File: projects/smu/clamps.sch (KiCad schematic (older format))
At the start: 39 parts, among them U401 DAC8734, U402 LM324, U404 LM324, U405 DG444

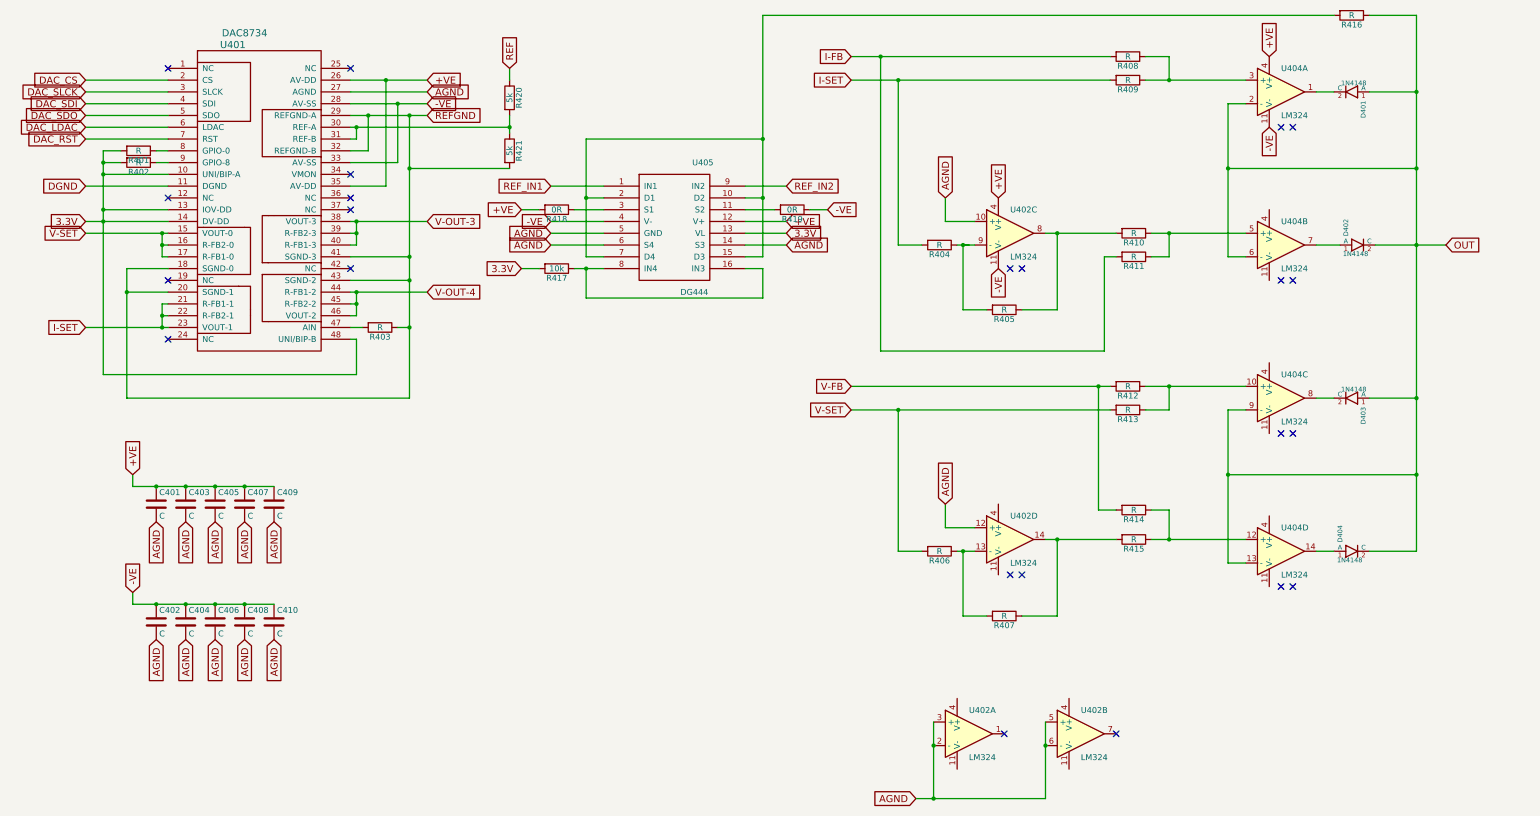
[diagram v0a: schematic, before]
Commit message: add output section
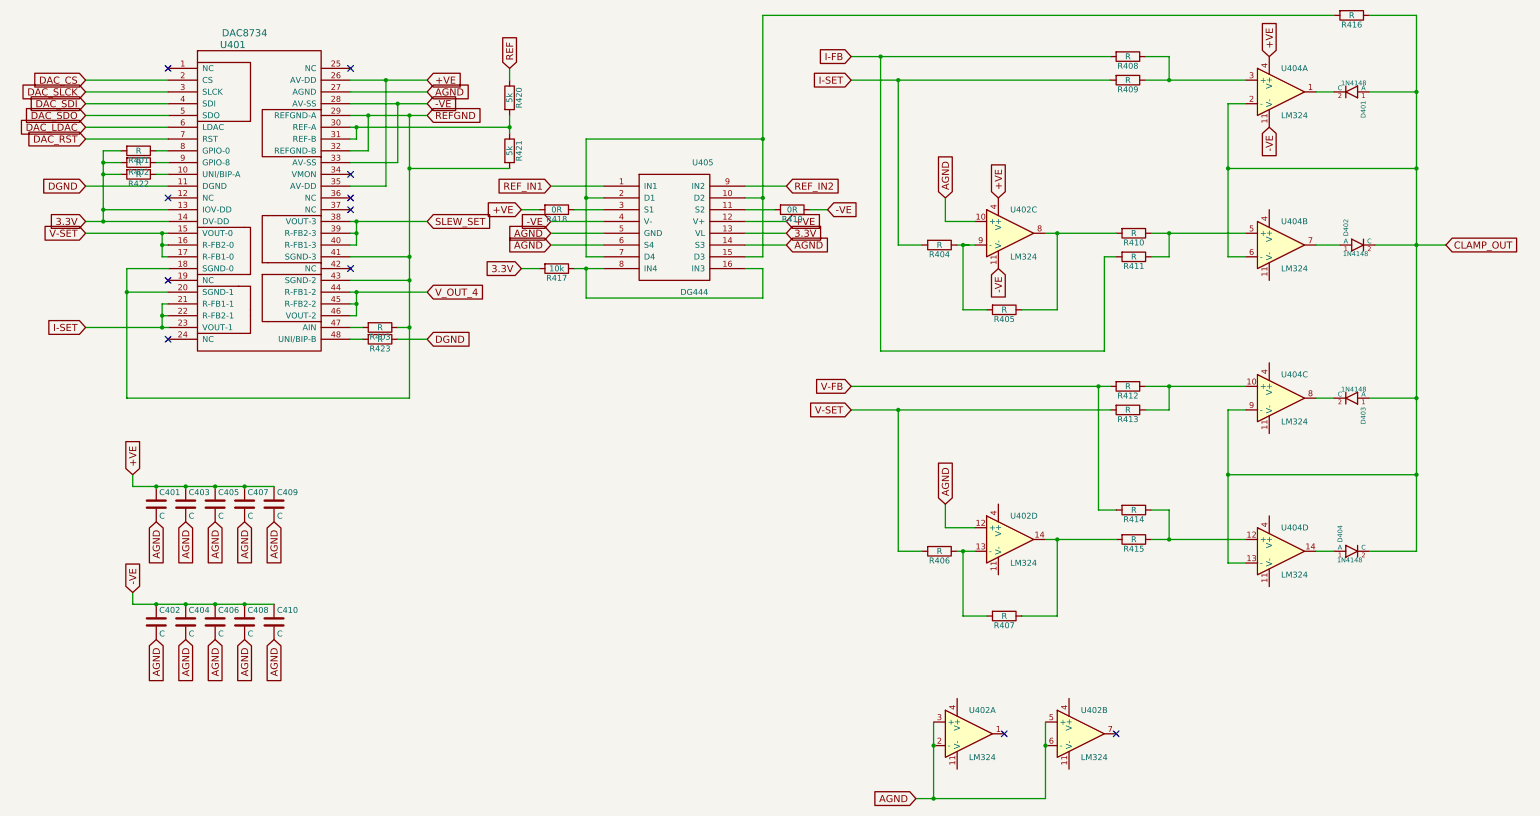
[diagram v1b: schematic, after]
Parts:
- added R422: R, symbol R
- added R423: R, Resistors_SMD:R_1206, symbol R
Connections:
- net 3.3V: now also R422.2; no longer U401.10 (UNI/BIP-A), U401.48 (UNI/BIP-B)
- net DGND: now also R423.1
- net OUT renamed CLAMP_OUT
- net V-OUT-3 renamed SLEW_SET
- net V-OUT-4 renamed V_OUT_4
- new net: R422.1, U401.10 (UNI/BIP-A)
- new net: R423.2, U401.48 (UNI/BIP-B)
- no-connect marks 23 -> 11
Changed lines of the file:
@@
 Text GLabel 1800 5050 1    60   Input ~ 0
 +VE
-NoConn ~ 11550 2100
-NoConn ~ 11650 2100
 $Comp
 L 1N4148 D401
@@
 	1    0    0    -1
 $EndComp
-NoConn ~ 11550 3400
-NoConn ~ 11650 3400
 $Comp
 L 1N4148 D402
@@
 -VE
 Text GLabel 12950 3100 2    60   Input ~ 0
-OUT
-NoConn ~ 11550 4700
-NoConn ~ 11650 4700
+CLAMP_OUT
 $Comp
 L 1N4148 D403
@@
 	-1   0    0    1
 $EndComp
-NoConn ~ 11550 6000
-NoConn ~ 11650 6000
 $Comp
 L 1N4148 D404
@@
 	0    1    1    0
 $EndComp
-NoConn ~ 9250 5900
-NoConn ~ 9350 5900
 $Comp
 L R R412
@@
 Text GLabel 9150 3300 3    60   Input ~ 0
 -VE
-NoConn ~ 9250 3300
-NoConn ~ 9350 3300
 Text GLabel 8700 2700 1    60   Input ~ 0
 AGND
@@
 V-SET
 Text GLabel 4300 2900 2    60   Input ~ 0
-V-OUT-3
+SLEW_SET
 Text GLabel 4300 3500 2    60   Input ~ 0
-V-OUT-4
+V_OUT_4
 $Comp
 L LM324 U402
@@
 	8700 2700 8700 2900
 Wire Wire Line
-	1550 2500 2100 2500
-Wire Wire Line
-	1550 2300 1550 4200
-Wire Wire Line
 	1550 2800 2100 2800
 Wire Wire Line
@@
 Connection ~ 3700 2100
 Connection ~ 3800 2000
-Wire Wire Line
-	1550 4200 3700 4200
-Wire Wire Line
-	3700 4200 3700 3900
-Wire Wire Line
-	3700 3900 3650 3900
 Connection ~ 1550 2800
 Wire Wire Line
-	3650 3200 4150 3200
+	4150 3200 3650 3200
 Wire Wire Line
 	4150 3400 3650 3400
@@
 Wire Wire Line
 	5000 1700 5000 1600
+$Comp
+L R R422
+U 1 1 58C42516
+P 1850 2500
+F 0 "R422" V 1930 2500 50  0000 C CNN
+F 1 "R" V 1850 2500 50  0000 C CNN
+F 2 "" V 1780 2500 50  0000 C CNN
+F 3 "" H 1850 2500 50  0000 C CNN
+	1    1850 2500
+	0    1    1    0
+$EndComp
+Wire Wire Line
+	1550 2500 1700 2500
+Wire Wire Line
+	2000 2500 2100 2500
+Text GLabel 4300 3900 2    60   Input ~ 0
+DGND
+Wire Wire Line
+	1550 2300 1550 2900
+$Comp
+L R R423
+U 1 1 58C441B3
+P 3900 3900
+F 0 "R423" V 3980 3900 50  0000 C CNN
+F 1 "R" V 3900 3900 50  0000 C CNN
+F 2 "Resistors_SMD:R_1206" V 3830 3900 50  0001 C CNN
+F 3 "" H 3900 3900 50  0000 C CNN
+	1    3900 3900
+	0    1    1    0
+$EndComp
+Wire Wire Line
+	3650 3900 3750 3900
+Wire Wire Line
+	4050 3900 4300 3900
 $EndSCHEMATC

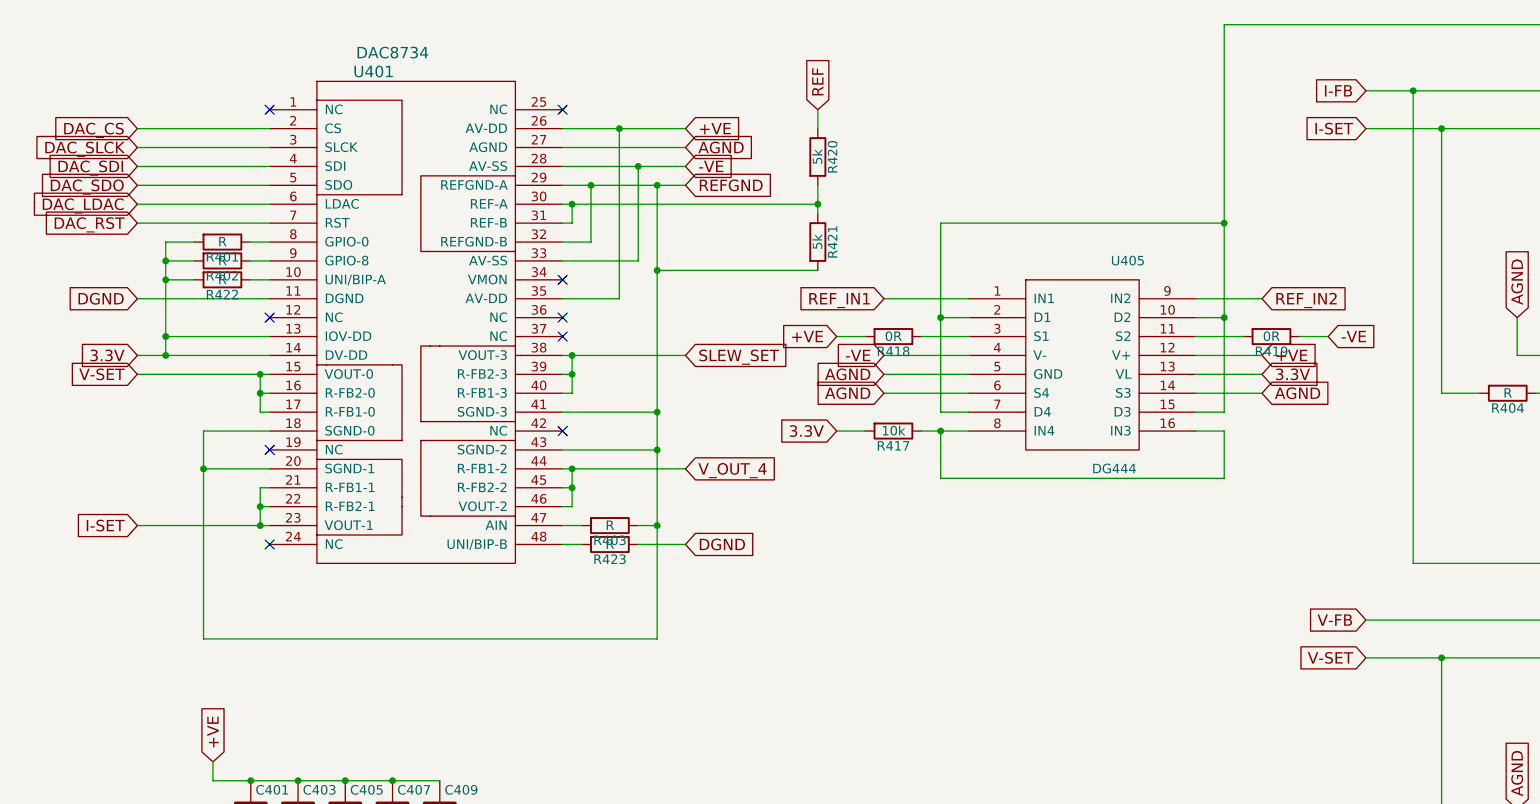
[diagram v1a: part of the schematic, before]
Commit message: split pin-headers into analog and digital
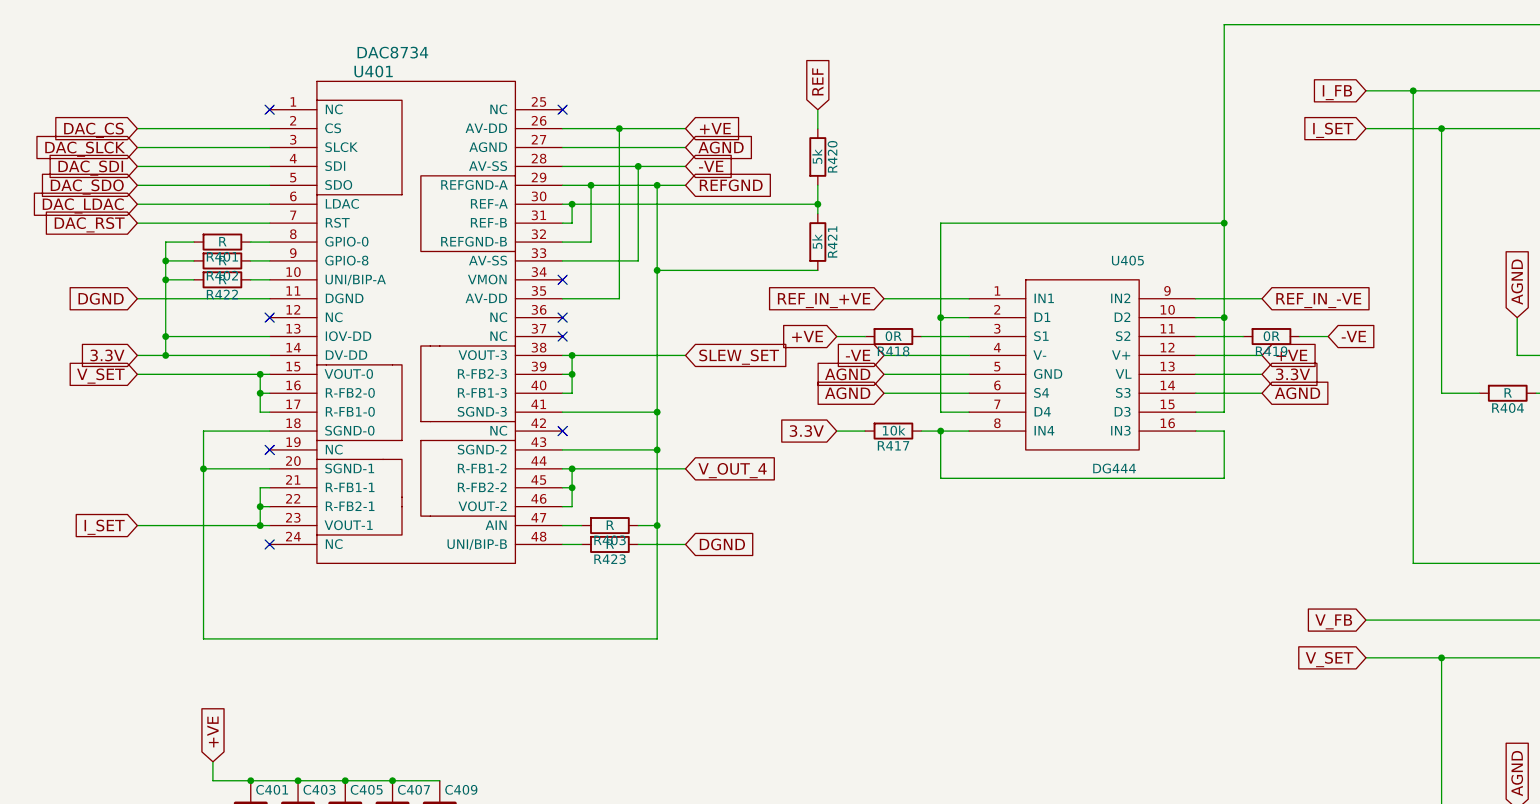
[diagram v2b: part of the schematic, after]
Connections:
- net I-FB renamed I_FB
- net I-SET renamed I_SET
- net REF_IN1 renamed REF_IN_+VE
- net REF_IN2 renamed REF_IN_-VE
- net V-FB renamed V_FB
- net V-SET renamed V_SET
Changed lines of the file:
@@
 $EndComp
 Text GLabel 7900 1500 0    60   Input ~ 0
-I-FB
+I_FB
 Text GLabel 7900 1700 0    60   Input ~ 0
-I-SET
+I_SET
 $Comp
 L R R408
@@
 AGND
 Text GLabel 7900 4500 0    60   Input ~ 0
-V-SET
+V_SET
 Text GLabel 7900 4300 0    60   Input ~ 0
-V-FB
+V_FB
 $Comp
 L R R405
@@
 NoConn ~ 2100 1600
 Text GLabel 1400 3800 0    60   Input ~ 0
-I-SET
+I_SET
 Text GLabel 1400 3000 0    60   Input ~ 0
-V-SET
+V_SET
 Text GLabel 4300 2900 2    60   Input ~ 0
 SLEW_SET
@@
 -VE
 Text GLabel 5350 2600 0    60   Input ~ 0
-REF_IN1
+REF_IN_+VE
 Text GLabel 7350 2600 2    60   Input ~ 0
-REF_IN2
+REF_IN_-VE
 Text GLabel 7350 3100 2    60   Input ~ 0
 AGND
